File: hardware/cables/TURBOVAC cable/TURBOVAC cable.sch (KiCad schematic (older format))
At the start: 4 parts, among them J1 RJ25, J2 DB9, J3 RJ25, J4 DB9

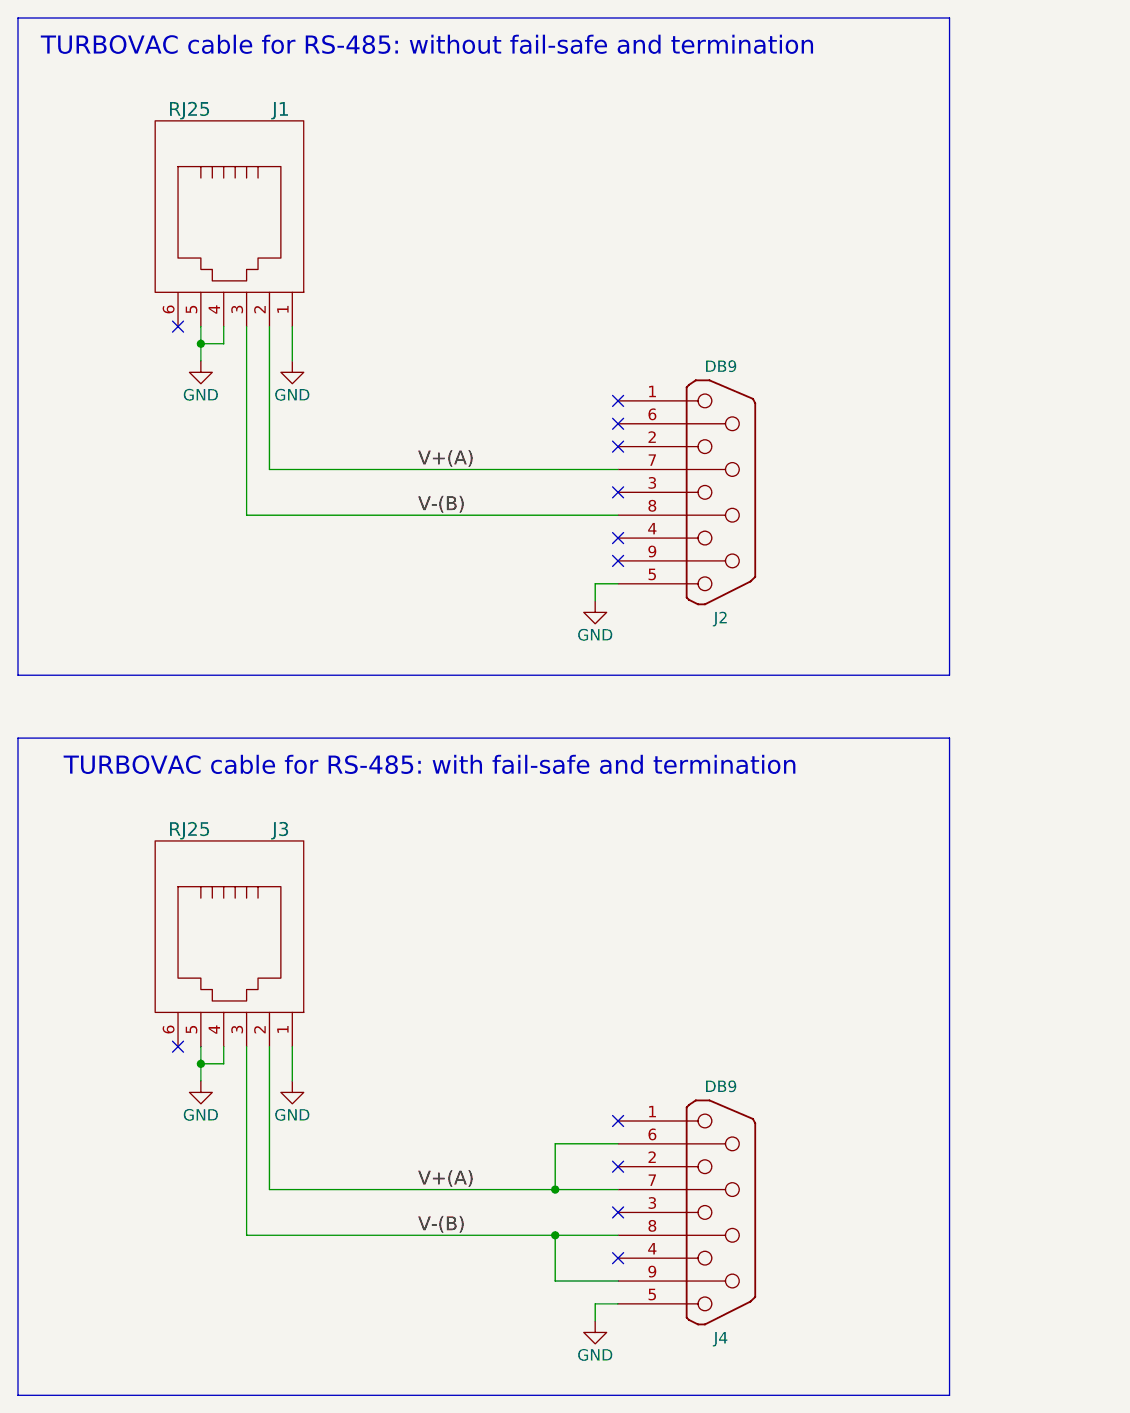
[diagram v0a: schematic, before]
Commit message: fixed Windows/Linux incompatibilities for PyDM 1.2 release
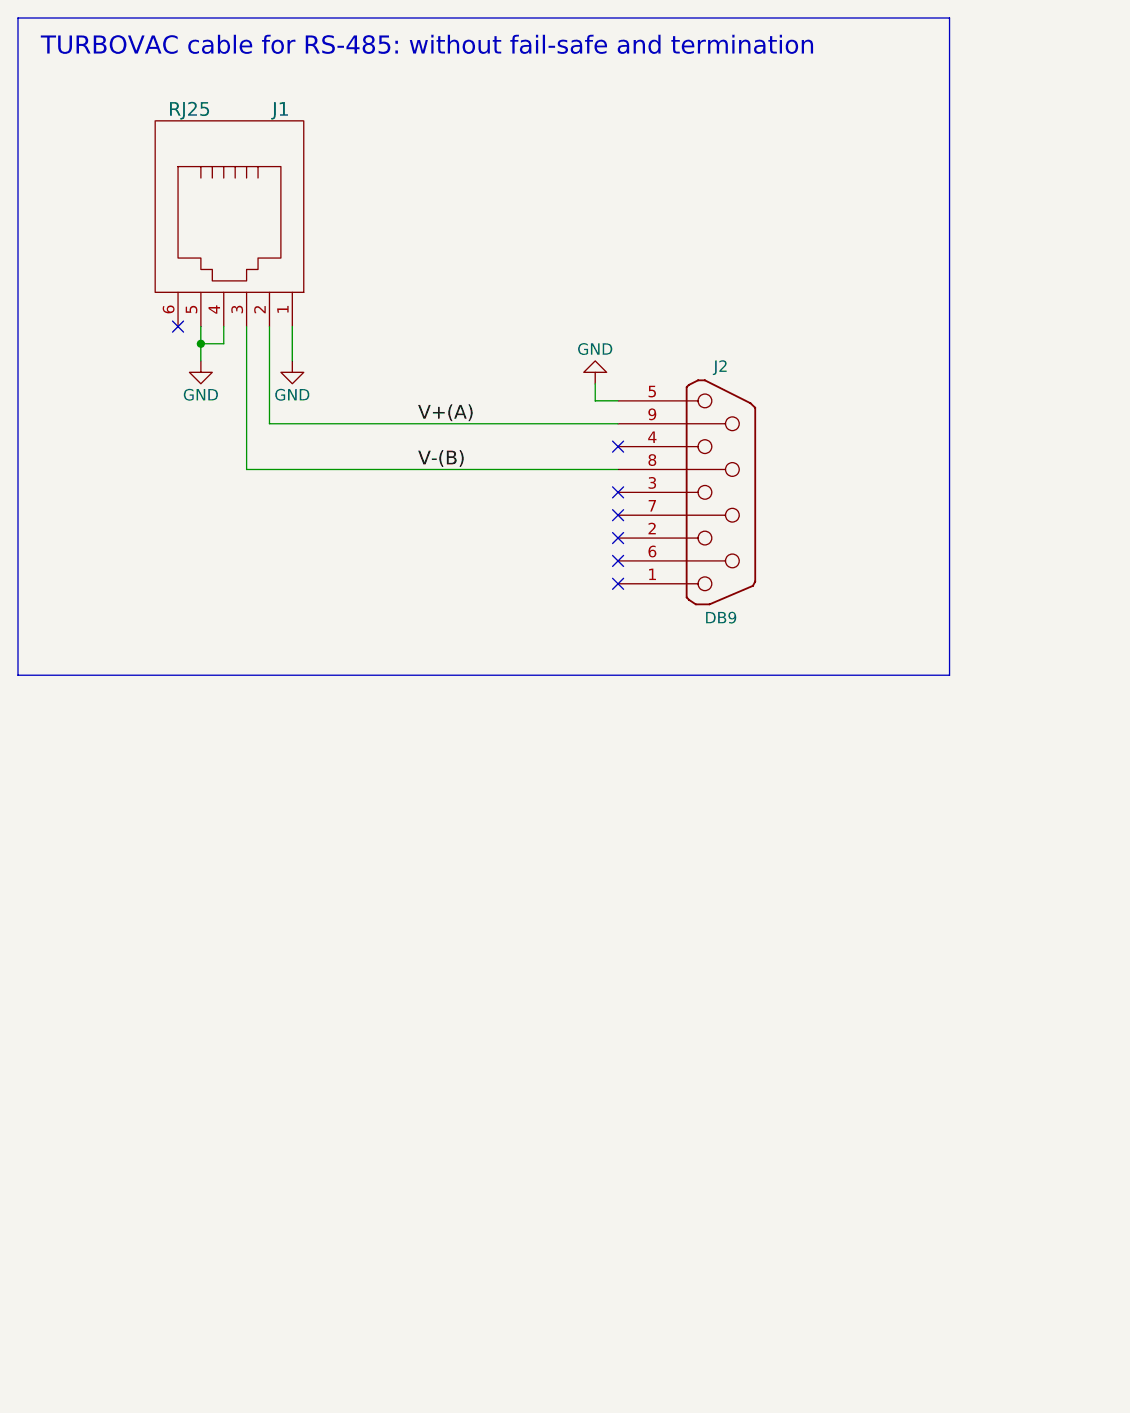
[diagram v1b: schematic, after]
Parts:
- removed J3: RJ25, symbol RJ25
- removed J4: DB9, symbol DB9
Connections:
- net V+(A): now also J2.9 (P9); no longer J2.7 (P7)
- no-connect marks 12 -> 7
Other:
- note removed: "TURBOVAC cable for RS-485: with fail-safe and termination"
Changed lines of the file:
@@
 TURBOVAC cable for RS-485: without fail-safe and termination
-$Comp
-L RJ25 J3
-U 1 1 5B2BA50F
-P 2450 4975
-F 0 "J3" H 2700 5475 60  0000 C CNN
-F 1 "RJ25" H 2300 5475 60  0000 C CNN
-F 2 "" H 2450 4975 60  0000 C CNN
-F 3 "" H 2450 4975 60  0000 C CNN
-	1    2450 4975
-	1    0    0    -1
-$EndComp
-$Comp
-L GND #PWR?
-U 1 1 5B2BA515
-P 2750 5575
-F 0 "#PWR?" H 2750 5325 50  0001 C CNN
-F 1 "GND" H 2750 5425 50  0000 C CNN
-F 2 "" H 2750 5575 50  0000 C CNN
-F 3 "" H 2750 5575 50  0000 C CNN
-	1    2750 5575
-	-1   0    0    -1
-$EndComp
-$Comp
-L GND #PWR?
-U 1 1 5B2BA51B
-P 2350 5575
-F 0 "#PWR?" H 2350 5325 50  0001 C CNN
-F 1 "GND" H 2350 5425 50  0000 C CNN
-F 2 "" H 2350 5575 50  0000 C CNN
-F 3 "" H 2350 5575 50  0000 C CNN
-	1    2350 5575
-	-1   0    0    -1
-$EndComp
-NoConn ~ 4175 5750
-$Comp
-L DB9 J4
-U 1 1 5B2BA522
-P 4625 6150
-F 0 "J4" H 4625 6700 50  0000 C CNN
-F 1 "DB9" H 4625 5600 50  0000 C CNN
-F 2 "" H 4625 6150 50  0000 C CNN
-F 3 "" H 4625 6150 50  0000 C CNN
-	1    4625 6150
-	1    0    0    1
-$EndComp
-NoConn ~ 4175 5950
-NoConn ~ 4175 6150
-NoConn ~ 4175 6350
-$Comp
-L GND #PWR?
-U 1 1 5B2BA52D
-P 4075 6625
-F 0 "#PWR?" H 4075 6375 50  0001 C CNN
-F 1 "GND" H 4075 6475 50  0000 C CNN
-F 2 "" H 4075 6625 50  0000 C CNN
-F 3 "" H 4075 6625 50  0000 C CNN
-	1    4075 6625
-	1    0    0    -1
-$EndComp
-Wire Wire Line
-	4175 6550 4075 6550
-Wire Wire Line
-	4075 6550 4075 6625
-Wire Wire Line
-	2750 5425 2750 5575
-Wire Wire Line
-	2350 5425 2350 5575
-NoConn ~ 2250 5425
-Text Label 3300 6050 0    60   ~ 0
-V+(A)
-Text Label 3300 6250 0    60   ~ 0
-V-(B)
-Wire Bus Line
-	1550 4075 1550 6950
-Wire Bus Line
-	1550 6950 5625 6950
-Wire Bus Line
-	5625 6950 5625 4075
-Wire Bus Line
-	5625 4075 1550 4075
-Text Notes 1750 4250 0    79   ~ 0
-TURBOVAC cable for RS-485: with fail-safe and termination
-Wire Wire Line
-	2450 5425 2450 5500
-Wire Wire Line
-	2450 5500 2350 5500
-Connection ~ 2350 5500
-Wire Wire Line
-	2550 5425 2550 6250
-Wire Wire Line
-	2550 6250 4175 6250
-Wire Wire Line
-	2650 5425 2650 6050
-Wire Wire Line
-	2650 6050 4175 6050
 $Comp
 L RJ25 J1
@@
 	-1   0    0    -1
 $EndComp
-NoConn ~ 4175 2600
+NoConn ~ 4175 3400
 $Comp
 L DB9 J2
@@
 F 3 "" H 4625 3000 50  0000 C CNN
 	1    4625 3000
-	1    0    0    1
+	1    0    0    -1
 $EndComp
+NoConn ~ 4175 3200
+NoConn ~ 4175 3000
 NoConn ~ 4175 2800
-NoConn ~ 4175 3000
-NoConn ~ 4175 3200
 $Comp
 L GND #PWR?
 U 1 1 5B2BA9ED
-P 4075 3475
-F 0 "#PWR?" H 4075 3225 50  0001 C CNN
-F 1 "GND" H 4075 3325 50  0000 C CNN
-F 2 "" H 4075 3475 50  0000 C CNN
-F 3 "" H 4075 3475 50  0000 C CNN
-	1    4075 3475
-	1    0    0    -1
+P 4075 2525
+F 0 "#PWR?" H 4075 2275 50  0001 C CNN
+F 1 "GND" H 4075 2375 50  0000 C CNN
+F 2 "" H 4075 2525 50  0000 C CNN
+F 3 "" H 4075 2525 50  0000 C CNN
+	1    4075 2525
+	1    0    0    1
 $EndComp
 Wire Wire Line
-	4175 3400 4075 3400
+	4175 2600 4075 2600
 Wire Wire Line
-	4075 3400 4075 3475
+	4075 2600 4075 2525
 Wire Wire Line
 	2750 2275 2750 2425
@@
 	2350 2275 2350 2425
 NoConn ~ 2250 2275
+Text Label 3300 2700 0    60   ~ 0
+V+(A)
 Text Label 3300 2900 0    60   ~ 0
-V+(A)
-Text Label 3300 3100 0    60   ~ 0
 V-(B)
 Wire Bus Line
@@
 	2450 2350 2350 2350
 Connection ~ 2350 2350
+NoConn ~ 4175 3300
 Wire Wire Line
-	2550 2275 2550 3100
+	2550 2275 2550 2900
 Wire Wire Line
-	2550 3100 4175 3100
+	2550 2900 4175 2900
 Wire Wire Line
-	2650 2275 2650 2900
+	2650 2275 2650 2700
 Wire Wire Line
-	2650 2900 4175 2900
-Wire Wire Line
-	4175 5850 3900 5850
-Wire Wire Line
-	3900 5850 3900 6050
-Connection ~ 3900 6050
-Wire Wire Line
-	4175 6450 3900 6450
-Wire Wire Line
-	3900 6450 3900 6250
-Connection ~ 3900 6250
-NoConn ~ 4175 2700
-NoConn ~ 4175 3300
+	2650 2700 4175 2700
+NoConn ~ 4175 3100
 $EndSCHEMATC
